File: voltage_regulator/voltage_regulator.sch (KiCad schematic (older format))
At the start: 5 parts

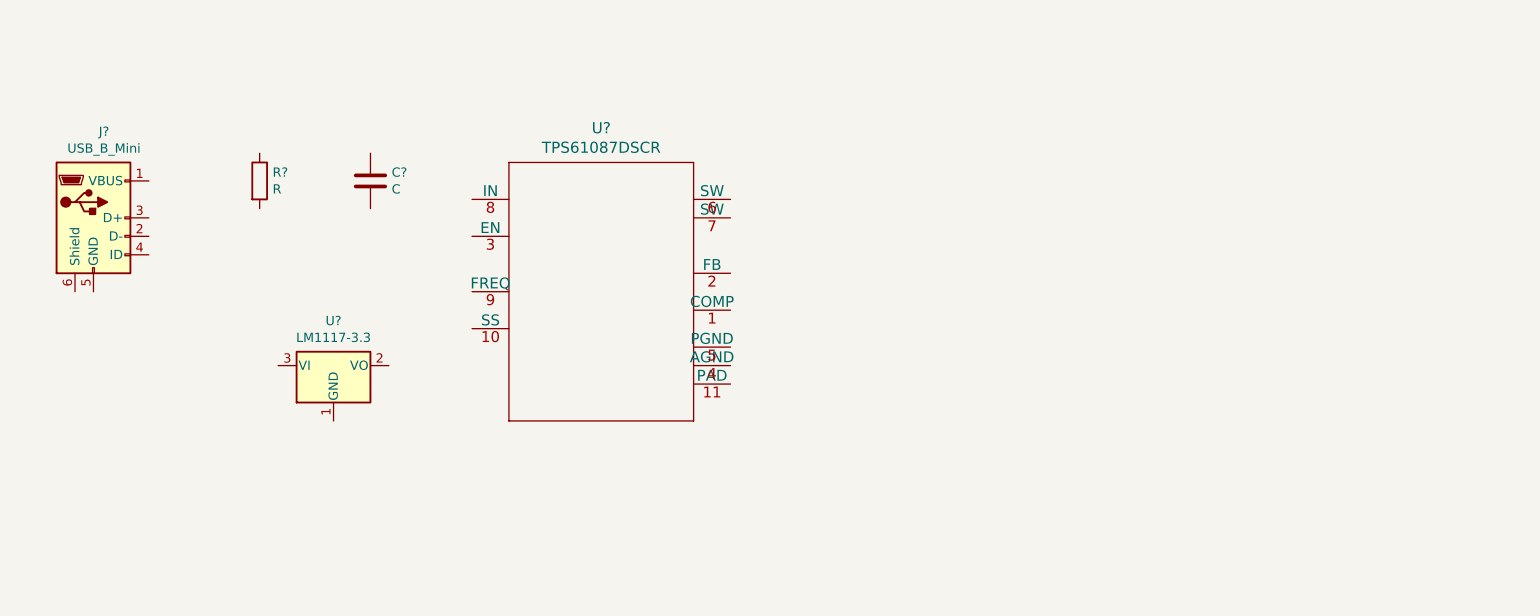
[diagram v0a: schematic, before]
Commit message: Finish the schematic of the Voltage
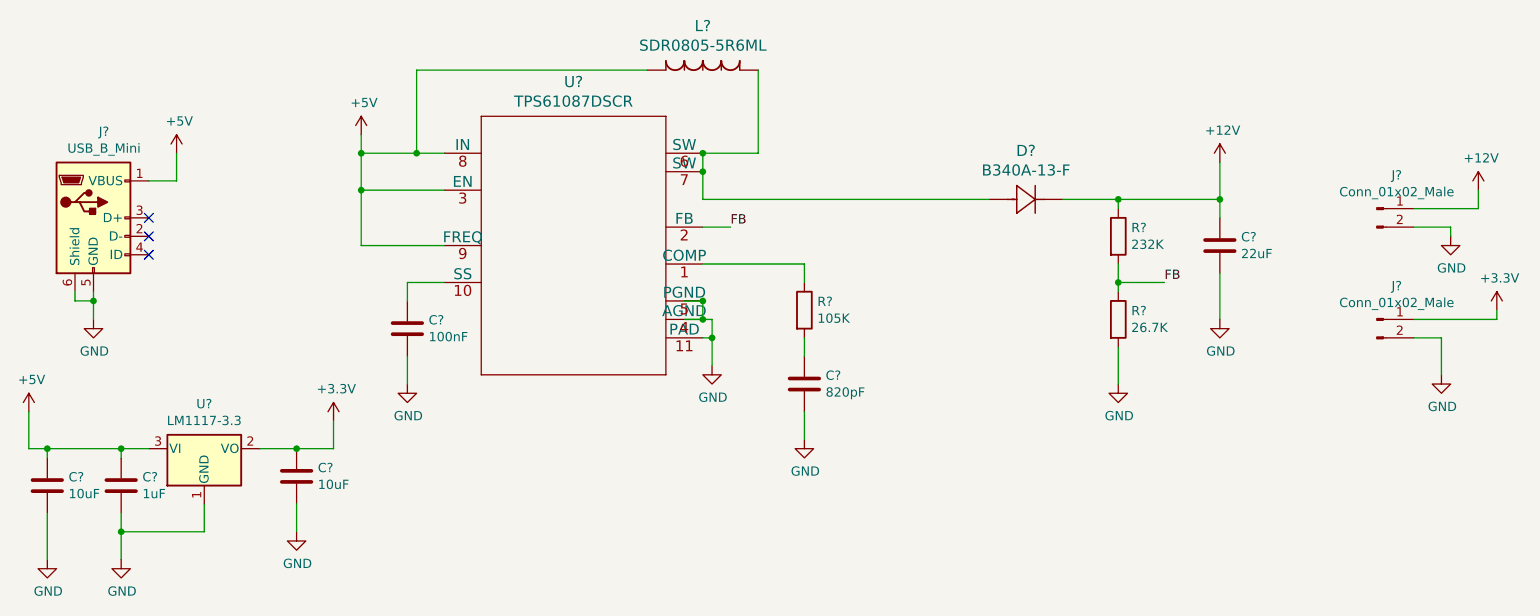
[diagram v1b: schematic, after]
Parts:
- added C?: 100nF, symbol Device:C
- added C?: 1uF, symbol Device:C
- added C? (x2): 10uF, symbol Device:C
- added C?: 22uF, symbol Device:C
- added D?: B340A-13-F, DIODE_SODB340_2P92X4P6_DIO, symbol D_B340A13F:B340A-13-F
- added J? (x2): Conn_01x02_Male, symbol Connector:Conn_01x02_Male
- added L?: SDR0805-5R6ML, IND_BOURNS_SDR0805, symbol L_SDR08055R6ML:SDR0805-5R6ML
- added R?: 105K, symbol Device:R
- added R?: 26.7K, symbol Device:R
- C?: value C -> 820pF
- R?: value R -> 232K
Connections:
- net labels added: +12V, +3.3V, +5V, FB, GND
- wire segments 0 -> 68
- no-connect marks 0 -> 3
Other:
- moved on the sheet: C?, R?, U?
